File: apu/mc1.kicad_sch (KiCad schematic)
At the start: 26 parts, among them U1 X818336-001

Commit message: Internal Connectors
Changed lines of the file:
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@@
 	(bus
 		(pts
-			(xy 36.83 22.86) (xy 41.91 22.86)
+			(xy 39.37 22.86) (xy 41.91 22.86)
 		)
 		(stroke
@@
 	(bus
 		(pts
-			(xy 252.73 22.86) (xy 257.81 22.86)
+			(xy 252.73 22.86) (xy 255.27 22.86)
 		)
 		(stroke
@@
 	(bus
 		(pts
-			(xy 133.35 22.86) (xy 138.43 22.86)
+			(xy 133.35 22.86) (xy 135.89 22.86)
 		)
 		(stroke
@@
 	(bus
 		(pts
-			(xy 156.21 20.32) (xy 161.29 20.32)
+			(xy 158.75 20.32) (xy 161.29 20.32)
 		)
 		(stroke
@@
 	(hierarchical_label "MC{SDRAM}"
 		(shape bidirectional)
-		(at 36.83 22.86 180)
+		(at 39.37 22.86 180)
 		(effects
 			(font
@@
 	(hierarchical_label "MC{SDRAM}"
 		(shape bidirectional)
-		(at 138.43 22.86 0)
+		(at 135.89 22.86 0)
 		(effects
 			(font
@@
 	(hierarchical_label "MD{SDRAM}"
 		(shape bidirectional)
-		(at 156.21 20.32 180)
+		(at 158.75 20.32 180)
 		(effects
 			(font
@@
 	(hierarchical_label "MD{SDRAM}"
 		(shape bidirectional)
-		(at 257.81 22.86 0)
+		(at 255.27 22.86 0)
 		(effects
 			(font

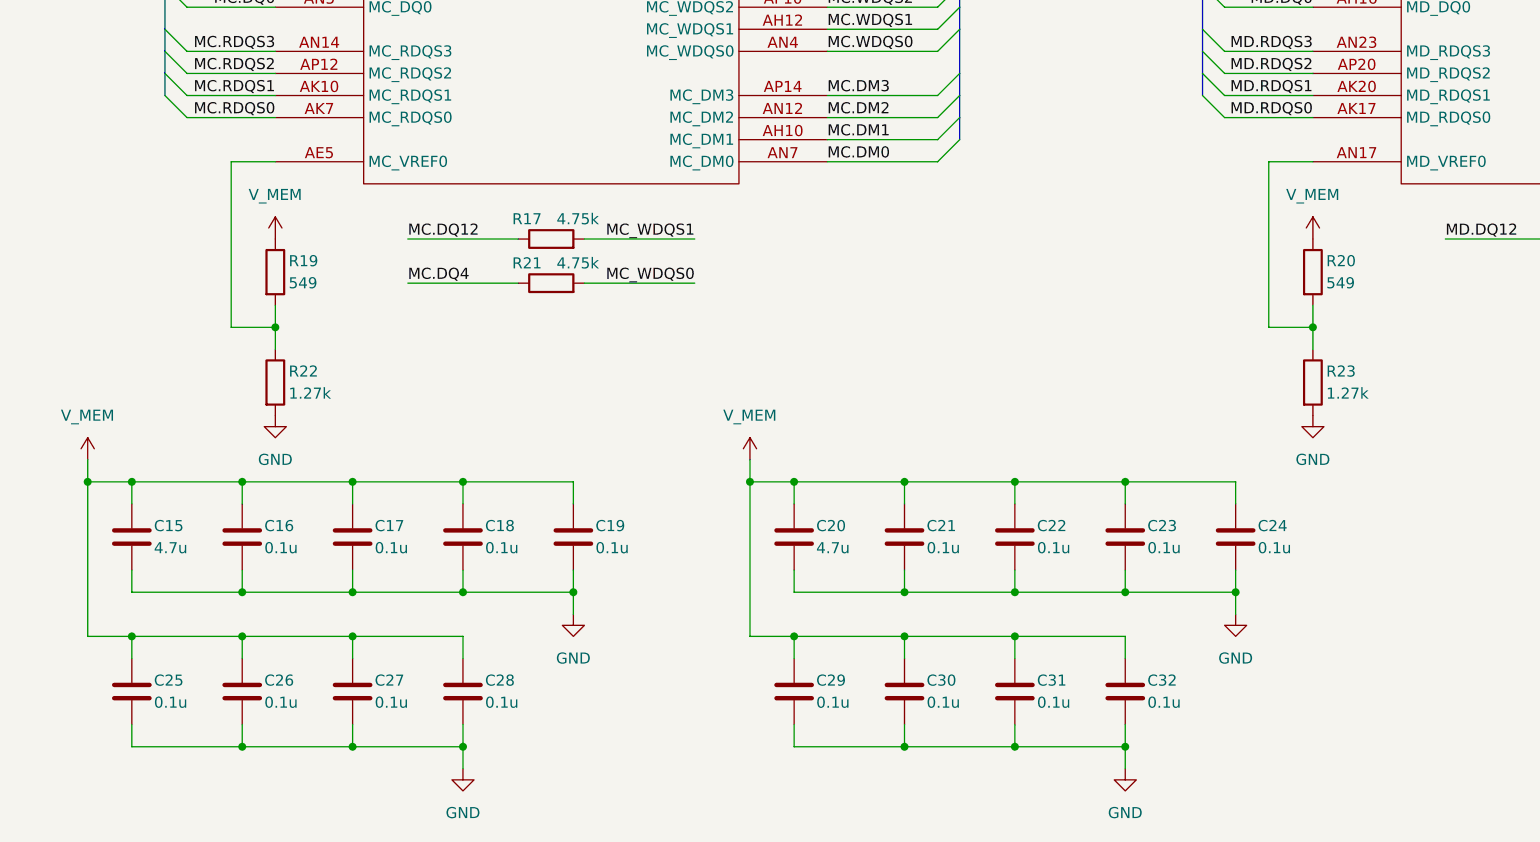
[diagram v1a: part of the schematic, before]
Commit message: Nand Flash, Sata Connectors and removing (hopefully) unnecessary things
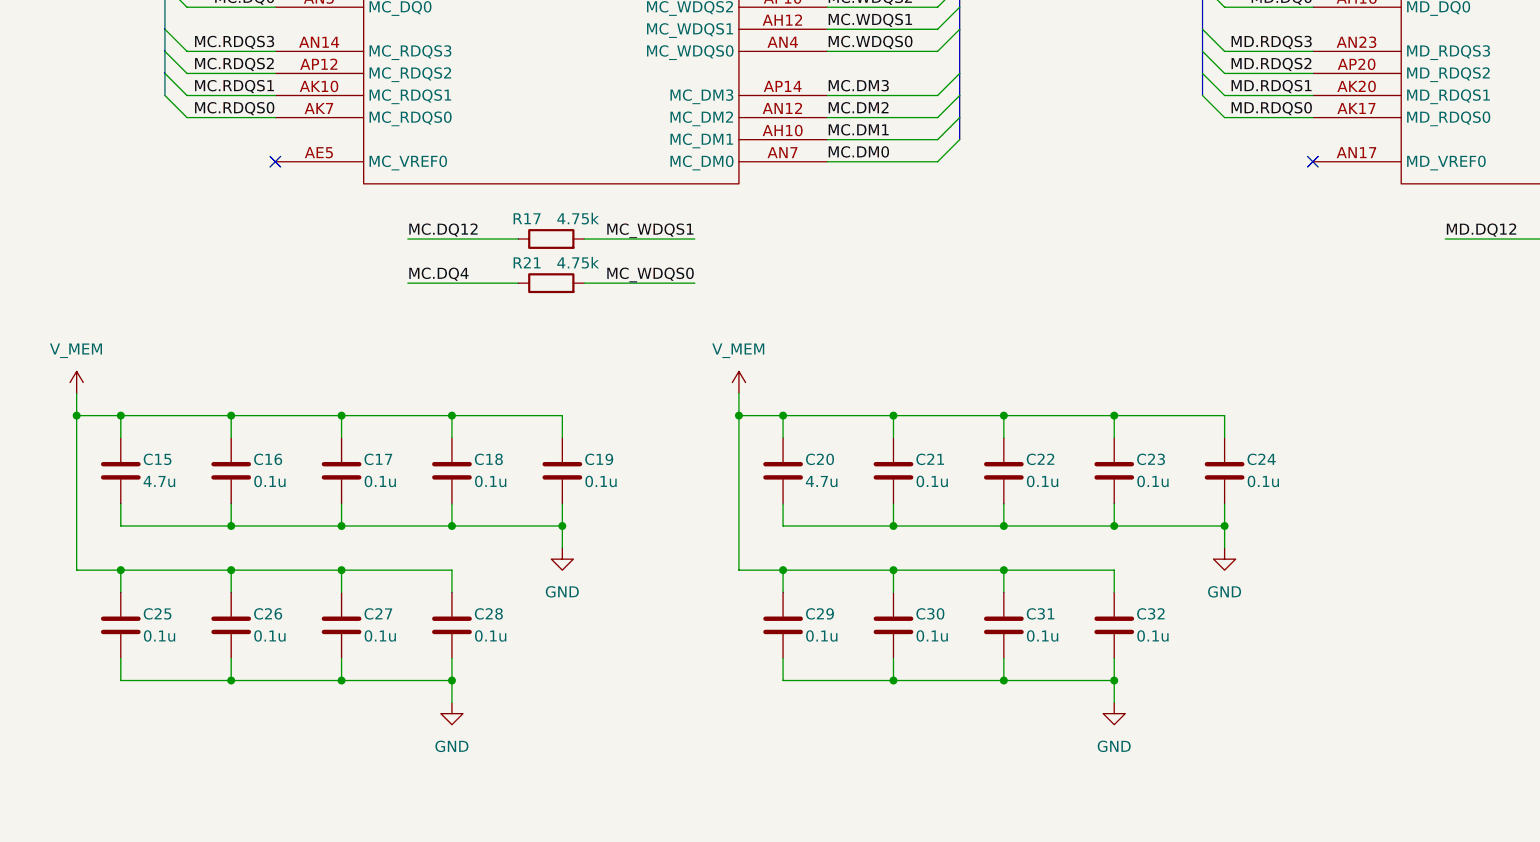
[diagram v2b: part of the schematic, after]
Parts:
- removed R19, R20: 549, symbol Device:R
- removed R22, R23: 1.27k, symbol Device:R
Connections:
- no-connect marks 0 -> 2
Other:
- moved on the sheet: C15, C16, C17, C18, C19, C20, C21, C22, C23, C24, C25, C26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

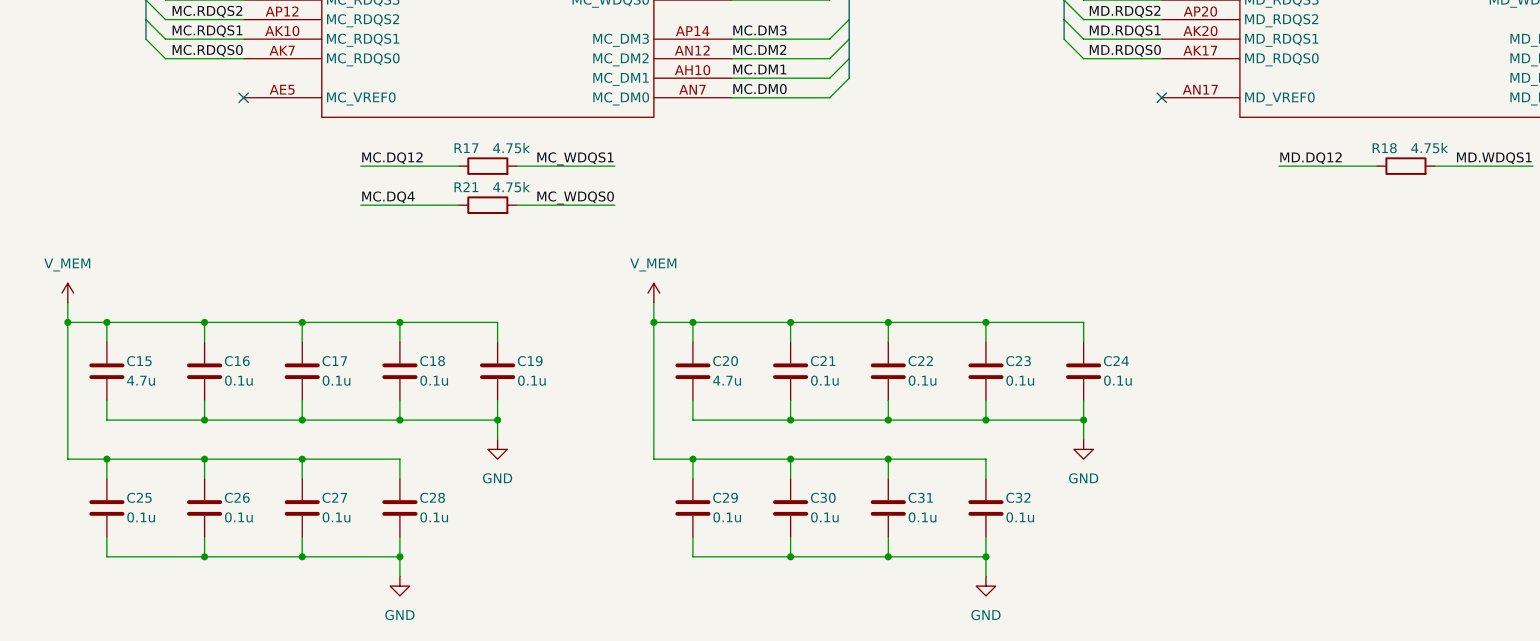
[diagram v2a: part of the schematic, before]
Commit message: Multipurpose and standby power rails, Reannotated schematic
Added V_1P2, V_1P8, V_5P0DUAL, V_EFUSE, V_GPUPCIE, V_3P3STBY and V_1P2STBY
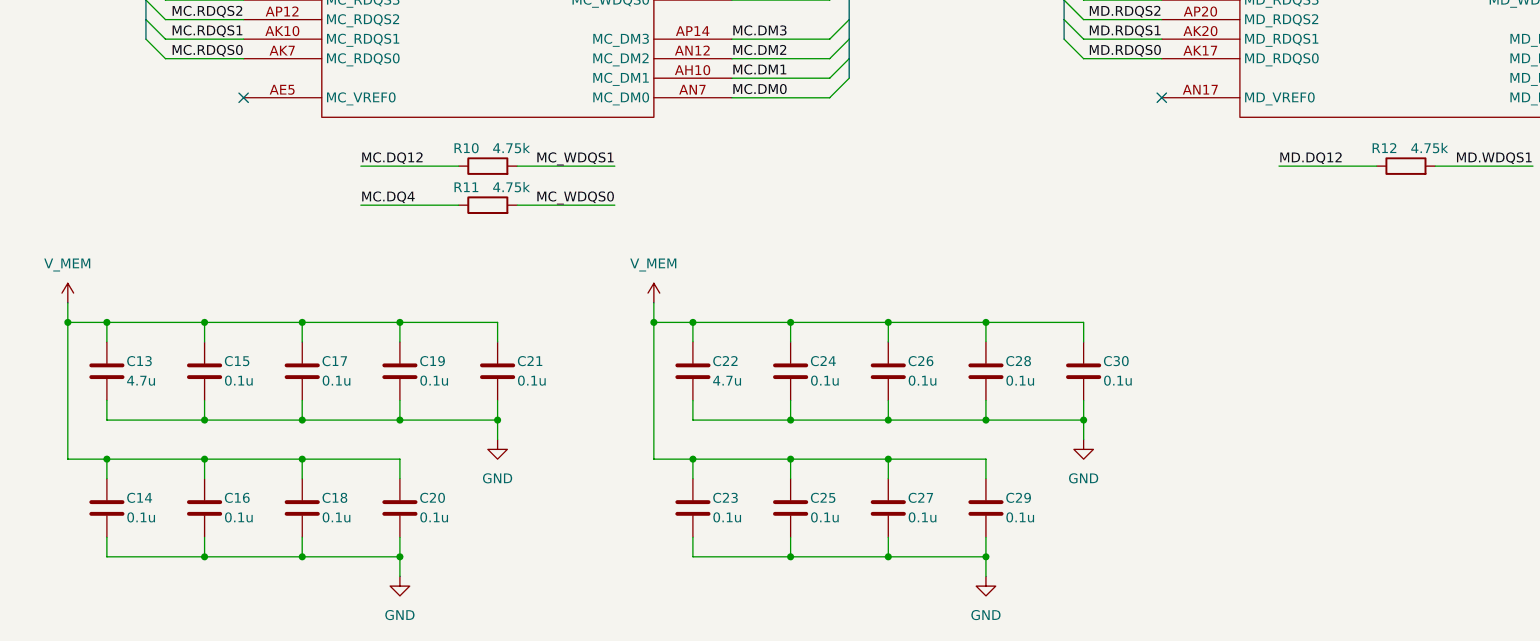
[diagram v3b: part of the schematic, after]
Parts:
- renumbered C15 to C13, C25 to C14, C16 to C15, C26 to C16, C27 to C18, C18 to C19, C28 to C20, C19 to C21, C20 to C22, C29 to C23, C21 to C24, C30 to C25, C22 to C26, C31 to C27, C23 to C28, C32 to C29, C24 to C30, R17 to R10, R21 to R11, R18 to R12
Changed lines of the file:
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@@
 		(on_board yes)
 		(dnp no)
-		(property "Reference" "R18"
+		(property "Reference" "R12"
 			(at 202.946 128.524 90)
 			(effects
@@
 			(project "StingBurst"
 				(path "/16640ecb-e4a4-4594-871b-70047bfba6e0/15d9acf0-ed9b-44aa-a266-2c44722c6abb/f48a7202-6ecc-46d0-a4b0-a02f14673ed1"
-					(reference "R18")
+					(reference "R12")
 					(unit 1)
 				)
@@
 		(on_board yes)
 		(dnp no)
-		(property "Reference" "C32"
+		(property "Reference" "C29"
 			(at 153.67 173.99 0)
 			(effects
@@
 			(project "StingBurst"
 				(path "/16640ecb-e4a4-4594-871b-70047bfba6e0/15d9acf0-ed9b-44aa-a266-2c44722c6abb/f48a7202-6ecc-46d0-a4b0-a02f14673ed1"
-					(reference "C32")
+					(reference "C29")
 					(unit 1)
 				)
@@
 		(on_board yes)
 		(dnp no)
-		(property "Reference" "R21"
+		(property "Reference" "R11"
 			(at 83.566 133.604 90)
 			(effects
@@
 			(project "StingBurst"
 				(path "/16640ecb-e4a4-4594-871b-70047bfba6e0/15d9acf0-ed9b-44aa-a266-2c44722c6abb/f48a7202-6ecc-46d0-a4b0-a02f14673ed1"
-					(reference "R21")
+					(reference "R11")
 					(unit 1)
 				)
@@
 		(on_board yes)
 		(dnp no)
-		(property "Reference" "C24"
+		(property "Reference" "C30"
 			(at 166.37 156.21 0)
 			(effects
@@
 			(project "StingBurst"
 				(path "/16640ecb-e4a4-4594-871b-70047bfba6e0/15d9acf0-ed9b-44aa-a266-2c44722c6abb/f48a7202-6ecc-46d0-a4b0-a02f14673ed1"
-					(reference "C24")
+					(reference "C30")
 					(unit 1)
 				)
@@
 		(on_board yes)
 		(dnp no)
-		(property "Reference" "C21"
+		(property "Reference" "C24"
 			(at 128.27 156.21 0)
 			(effects
@@
 			(project "StingBurst"
 				(path "/16640ecb-e4a4-4594-871b-70047bfba6e0/15d9acf0-ed9b-44aa-a266-2c44722c6abb/f48a7202-6ecc-46d0-a4b0-a02f14673ed1"
-					(reference "C21")
+					(reference "C24")
 					(unit 1)
 				)
@@
 		(dnp no)
 		(fields_autoplaced yes)
-		(property "Reference" "#PWR025"
+		(property "Reference" "#PWR016"
 			(at 163.83 172.72 0)
 			(effects
@@
 			(project "StingBurst"
 				(path "/16640ecb-e4a4-4594-871b-70047bfba6e0/15d9acf0-ed9b-44aa-a266-2c44722c6abb/f48a7202-6ecc-46d0-a4b0-a02f14673ed1"
-					(reference "#PWR025")
+					(reference "#PWR016")
 					(unit 1)
 				)
@@
 		(on_board yes)
 		(dnp no)
-		(property "Reference" "C26"
+		(property "Reference" "C16"
 			(at 52.07 173.99 0)
 			(effects
@@
 			(project "StingBurst"
 				(path "/16640ecb-e4a4-4594-871b-70047bfba6e0/15d9acf0-ed9b-44aa-a266-2c44722c6abb/f48a7202-6ecc-46d0-a4b0-a02f14673ed1"
-					(reference "C26")
+					(reference "C16")
 					(unit 1)
 				)
@@
 		(on_board yes)
 		(dnp no)
-		(property "Reference" "C23"
+		(property "Reference" "C28"
 			(at 153.67 156.21 0)
 			(effects
@@
 			(project "StingBurst"
 				(path "/16640ecb-e4a4-4594-871b-70047bfba6e0/15d9acf0-ed9b-44aa-a266-2c44722c6abb/f48a7202-6ecc-46d0-a4b0-a02f14673ed1"
-					(reference "C23")
+					(reference "C28")
 					(unit 1)
 				)
@@
 		(dnp no)
 		(fields_autoplaced yes)
-		(property "Reference" "#PWR027"
+		(property "Reference" "#PWR015"
 			(at 151.13 190.5 0)
 			(effects
@@
 			(project "StingBurst"
 				(path "/16640ecb-e4a4-4594-871b-70047bfba6e0/15d9acf0-ed9b-44aa-a266-2c44722c6abb/f48a7202-6ecc-46d0-a4b0-a02f14673ed1"
-					(reference "#PWR027")
+					(reference "#PWR015")
 					(unit 1)
 				)
@@
 		(on_board yes)
 		(dnp no)
-		(property "Reference" "C20"
+		(property "Reference" "C22"
 			(at 115.57 156.21 0)
 			(effects
@@
 			(project "StingBurst"
 				(path "/16640ecb-e4a4-4594-871b-70047bfba6e0/15d9acf0-ed9b-44aa-a266-2c44722c6abb/f48a7202-6ecc-46d0-a4b0-a02f14673ed1"
-					(reference "C20")
+					(reference "C22")
 					(unit 1)
 				)
@@
 		(on_board yes)
 		(dnp no)
-		(property "Reference" "C25"
+		(property "Reference" "C14"
 			(at 39.37 173.99 0)
 			(effects
@@
 			(project "StingBurst"
 				(path "/16640ecb-e4a4-4594-871b-70047bfba6e0/15d9acf0-ed9b-44aa-a266-2c44722c6abb/f48a7202-6ecc-46d0-a4b0-a02f14673ed1"
-					(reference "C25")
+					(reference "C14")
 					(unit 1)
 				)
@@
 		(on_board yes)
 		(dnp no)
-		(property "Reference" "C28"
+		(property "Reference" "C20"
 			(at 77.47 173.99 0)
 			(effects
@@
 			(project "StingBurst"
 				(path "/16640ecb-e4a4-4594-871b-70047bfba6e0/15d9acf0-ed9b-44aa-a266-2c44722c6abb/f48a7202-6ecc-46d0-a4b0-a02f14673ed1"
-					(reference "C28")
+					(reference "C20")
 					(unit 1)
 				)
@@
 		(on_board yes)
 		(dnp no)
-		(property "Reference" "C15"
+		(property "Reference" "C13"
 			(at 39.37 156.21 0)
 			(effects
@@
 			(project "StingBurst"
 				(path "/16640ecb-e4a4-4594-871b-70047bfba6e0/15d9acf0-ed9b-44aa-a266-2c44722c6abb/f48a7202-6ecc-46d0-a4b0-a02f14673ed1"
-					(reference "C15")
+					(reference "C13")
 					(unit 1)
 				)
@@
 		(on_board yes)
 		(dnp no)
-		(property "Reference" "C27"
+		(property "Reference" "C18"
 			(at 64.77 173.99 0)
 			(effects
@@
 			(project "StingBurst"
 				(path "/16640ecb-e4a4-4594-871b-70047bfba6e0/15d9acf0-ed9b-44aa-a266-2c44722c6abb/f48a7202-6ecc-46d0-a4b0-a02f14673ed1"
-					(reference "C27")
+					(reference "C18")
 					(unit 1)
 				)
@@
 		(dnp no)
 		(fields_autoplaced yes)
-		(property "Reference" "#PWR026"
+		(property "Reference" "#PWR012"
 			(at 74.93 190.5 0)
 			(effects
@@
 			(project "StingBurst"
 				(path "/16640ecb-e4a4-4594-871b-70047bfba6e0/15d9acf0-ed9b-44aa-a266-2c44722c6abb/f48a7202-6ecc-46d0-a4b0-a02f14673ed1"
-					(reference "#PWR026")
+					(reference "#PWR012")
 					(unit 1)
 				)
@@
 		(on_board yes)
 		(dnp no)
-		(property "Reference" "#PWR023"
+		(property "Reference" "#PWR014"
 			(at 107.95 152.4 0)
 			(effects
@@
 			(project "StingBurst"
 				(path "/16640ecb-e4a4-4594-871b-70047bfba6e0/15d9acf0-ed9b-44aa-a266-2c44722c6abb/f48a7202-6ecc-46d0-a4b0-a02f14673ed1"
-					(reference "#PWR023")
+					(reference "#PWR014")
 					(unit 1)
 				)
@@
 		(on_board yes)
 		(dnp no)
-		(property "Reference" "C19"
+		(property "Reference" "C21"
 			(at 90.17 156.21 0)
 			(effects
@@
 			(project "StingBurst"
 				(path "/16640ecb-e4a4-4594-871b-70047bfba6e0/15d9acf0-ed9b-44aa-a266-2c44722c6abb/f48a7202-6ecc-46d0-a4b0-a02f14673ed1"
-					(reference "C19")
+					(reference "C21")
 					(unit 1)
 				)
@@
 		(on_board yes)
 		(dnp no)
-		(property "Reference" "C29"
+		(property "Reference" "C23"
 			(at 115.57 173.99 0)
 			(effects
@@
 			(project "StingBurst"
 				(path "/16640ecb-e4a4-4594-871b-70047bfba6e0/15d9acf0-ed9b-44aa-a266-2c44722c6abb/f48a7202-6ecc-46d0-a4b0-a02f14673ed1"
-					(reference "C29")
+					(reference "C23")
 					(unit 1)
 				)
@@
 		(on_board yes)
 		(dnp no)
-		(property "Reference" "R17"
+		(property "Reference" "R10"
 			(at 83.566 128.524 90)
 			(effects
@@
 			(project "StingBurst"
 				(path "/16640ecb-e4a4-4594-871b-70047bfba6e0/15d9acf0-ed9b-44aa-a266-2c44722c6abb/f48a7202-6ecc-46d0-a4b0-a02f14673ed1"
-					(reference "R17")
+					(reference "R10")
 					(unit 1)
 				)
@@
 		(on_board yes)
 		(dnp no)
-		(property "Reference" "C18"
+		(property "Reference" "C19"
 			(at 77.47 156.21 0)
 			(effects
@@
 			(project "StingBurst"
 				(path "/16640ecb-e4a4-4594-871b-70047bfba6e0/15d9acf0-ed9b-44aa-a266-2c44722c6abb/f48a7202-6ecc-46d0-a4b0-a02f14673ed1"
-					(reference "C18")
+					(reference "C19")
 					(unit 1)
 				)
@@
 		(on_board yes)
 		(dnp no)
-		(property "Reference" "C31"
+		(property "Reference" "C27"
 			(at 140.97 173.99 0)
 			(effects
@@
 			(project "StingBurst"
 				(path "/16640ecb-e4a4-4594-871b-70047bfba6e0/15d9acf0-ed9b-44aa-a266-2c44722c6abb/f48a7202-6ecc-46d0-a4b0-a02f14673ed1"
-					(reference "C31")
+					(reference "C27")
 					(unit 1)
 				)
@@
 		(on_board yes)
 		(dnp no)
-		(property "Reference" "C30"
+		(property "Reference" "C25"
 			(at 128.27 173.99 0)
 			(effects
@@
 			(project "StingBurst"
 				(path "/16640ecb-e4a4-4594-871b-70047bfba6e0/15d9acf0-ed9b-44aa-a266-2c44722c6abb/f48a7202-6ecc-46d0-a4b0-a02f14673ed1"
-					(reference "C30")
+					(reference "C25")
 					(unit 1)
 				)
@@
 		(on_board yes)
 		(dnp no)
-		(property "Reference" "C22"
+		(property "Reference" "C26"
 			(at 140.97 156.21 0)
 			(effects
@@
 			(project "StingBurst"
 				(path "/16640ecb-e4a4-4594-871b-70047bfba6e0/15d9acf0-ed9b-44aa-a266-2c44722c6abb/f48a7202-6ecc-46d0-a4b0-a02f14673ed1"
-					(reference "C22")
+					(reference "C26")
 					(unit 1)
 				)
@@
 		(on_board yes)
 		(dnp no)
-		(property "Reference" "#PWR022"
+		(property "Reference" "#PWR011"
 			(at 31.75 152.4 0)
 			(effects
@@
 			(project "StingBurst"
 				(path "/16640ecb-e4a4-4594-871b-70047bfba6e0/15d9acf0-ed9b-44aa-a266-2c44722c6abb/f48a7202-6ecc-46d0-a4b0-a02f14673ed1"
-					(reference "#PWR022")
+					(reference "#PWR011")
 					(unit 1)
 				)
@@
 		(on_board yes)
 		(dnp no)
-		(property "Reference" "C16"
+		(property "Reference" "C15"
 			(at 52.07 156.21 0)
 			(effects
@@
 			(project "StingBurst"
 				(path "/16640ecb-e4a4-4594-871b-70047bfba6e0/15d9acf0-ed9b-44aa-a266-2c44722c6abb/f48a7202-6ecc-46d0-a4b0-a02f14673ed1"
-					(reference "C16")
+					(reference "C15")
 					(unit 1)
 				)
@@
 		(dnp no)
 		(fields_autoplaced yes)
-		(property "Reference" "#PWR024"
+		(property "Reference" "#PWR013"
 			(at 87.63 172.72 0)
 			(effects
@@
 			(project "StingBurst"
 				(path "/16640ecb-e4a4-4594-871b-70047bfba6e0/15d9acf0-ed9b-44aa-a266-2c44722c6abb/f48a7202-6ecc-46d0-a4b0-a02f14673ed1"
-					(reference "#PWR024")
+					(reference "#PWR013")
 					(unit 1)
 				)
